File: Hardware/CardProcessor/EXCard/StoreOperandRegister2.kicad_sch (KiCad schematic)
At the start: 2 parts, among them U14 74ABT16374

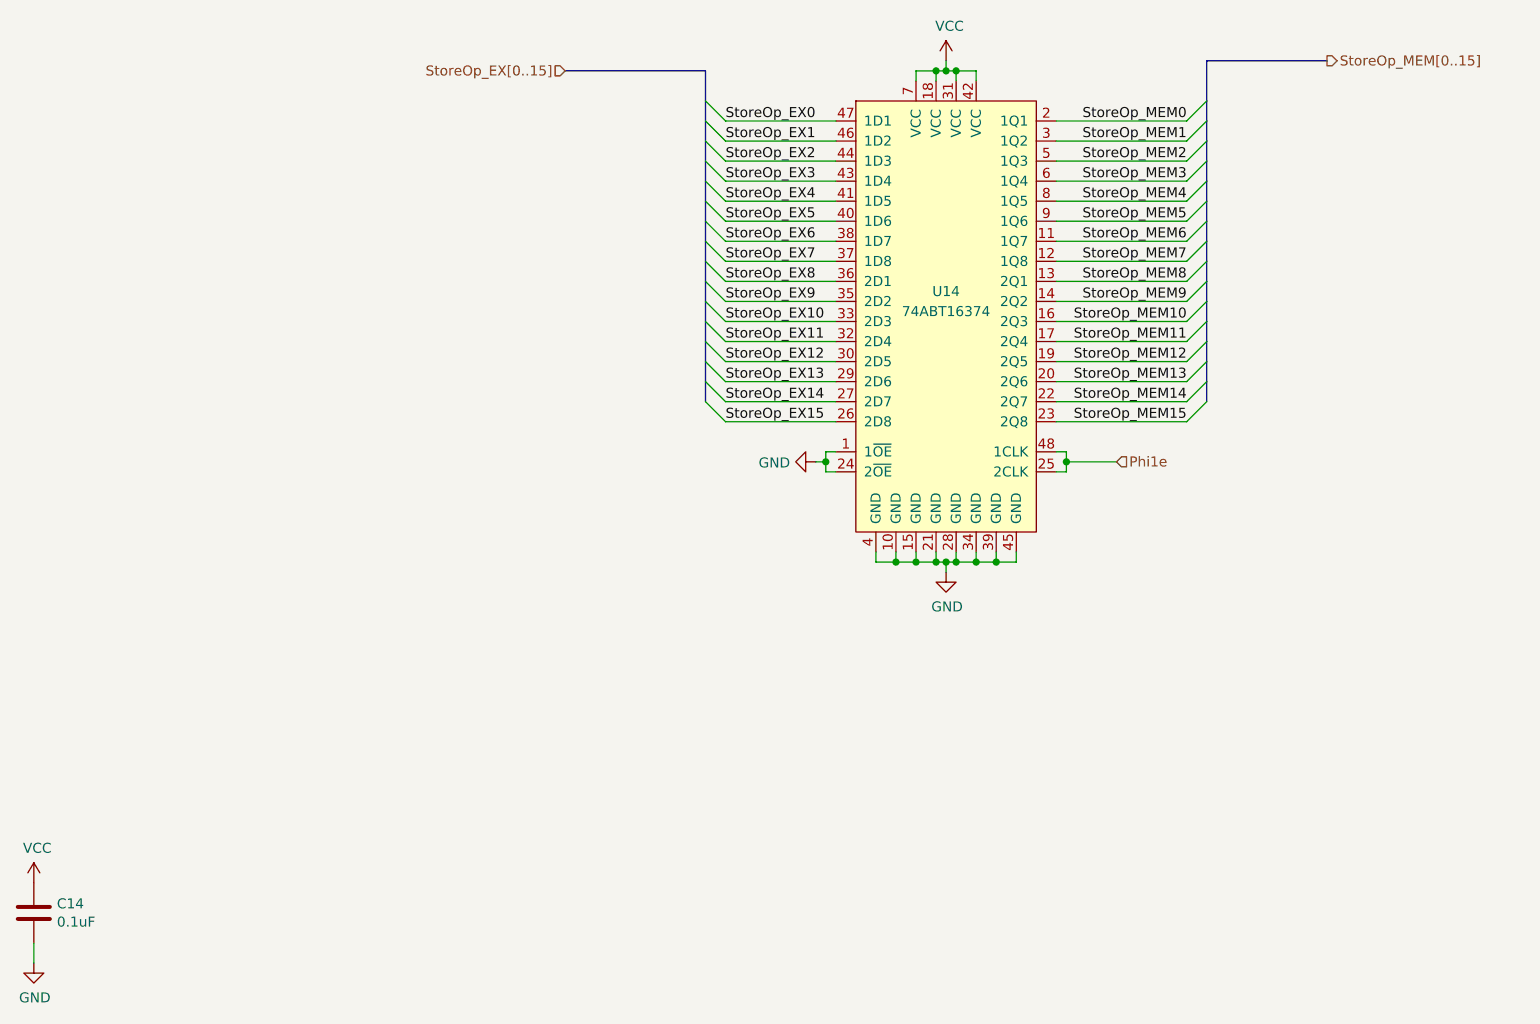
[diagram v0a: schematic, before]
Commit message: Add Turtle16Computer, a KiCad project which has schematics for the computer as a whole
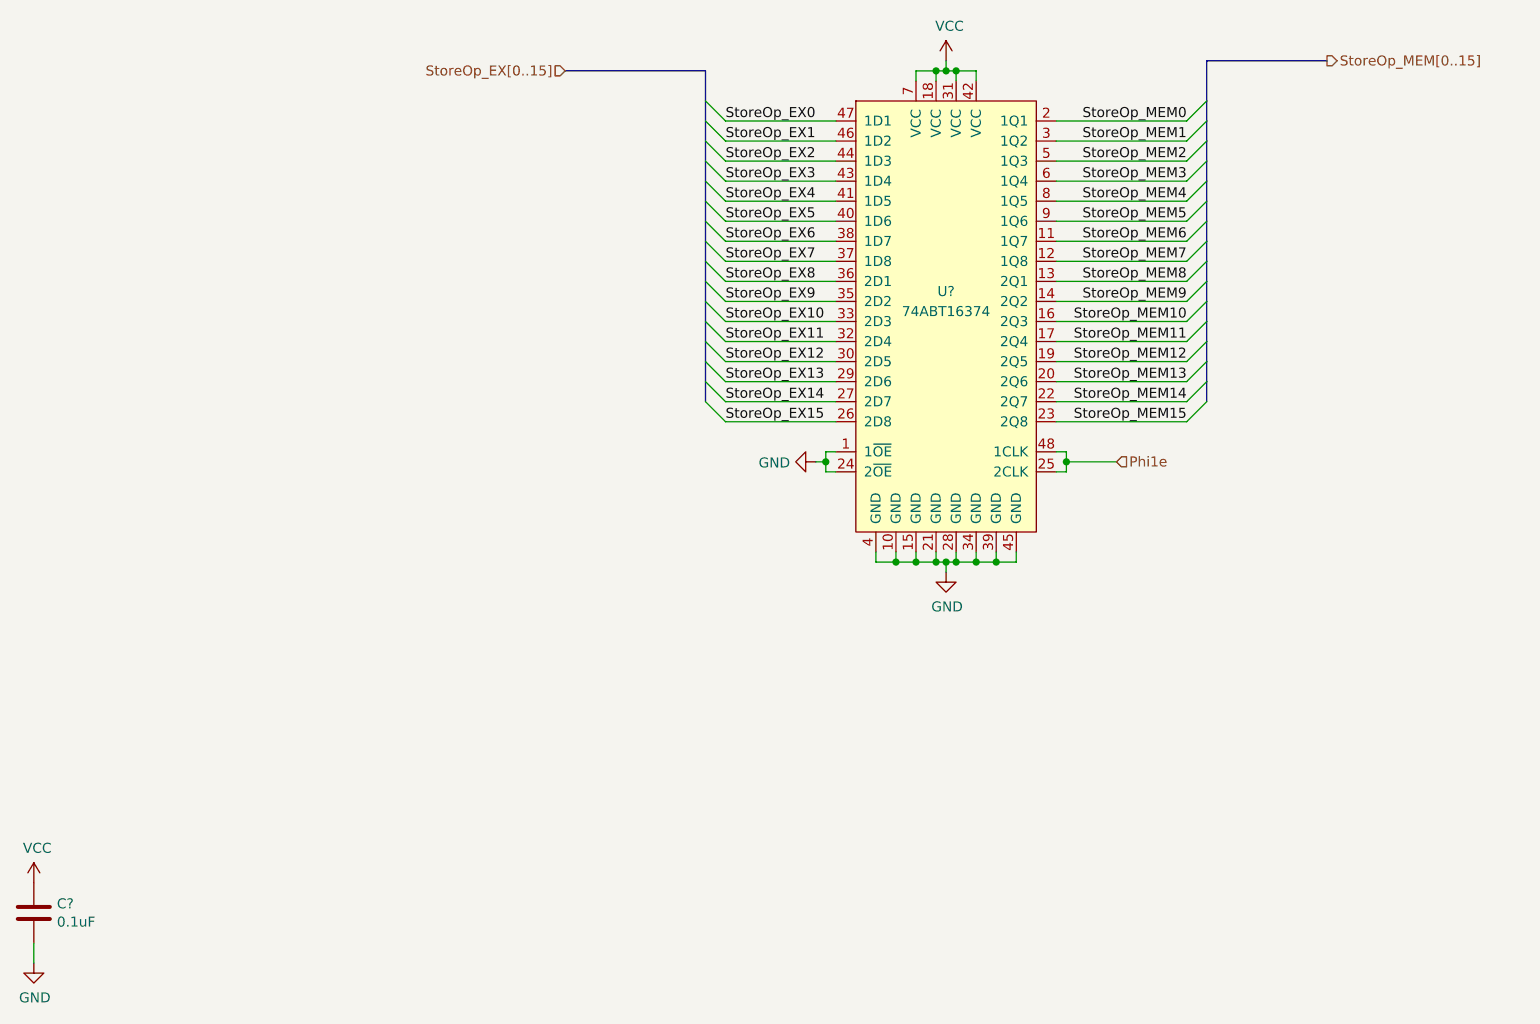
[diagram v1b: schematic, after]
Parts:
- renumbered C14 to C?, U14 to U?
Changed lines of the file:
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@@
 		(on_board yes)
 		(dnp no)
-		(property "Reference" "C14"
+		(property "Reference" "C?"
 			(at 32.131 177.9016 0)
 			(effects
@@
 		(instances
 			(project "EXModule"
-				(path "/83c5181e-f5ee-453c-ae5c-d7256ba8837d/43096b5e-2581-4688-8be9-9209d6e0ed88/00000000-0000-0000-0000-00005fd8d6fe"
-					(reference "C14")
+				(path "/83c5181e-f5ee-453c-ae5c-d7256ba8837d/637456a4-4ee5-48ca-bb06-9734ef3462ed/00000000-0000-0000-0000-00005fd8d6fe"
+					(reference "C?")
 					(unit 1)
 				)
@@
 		(on_board yes)
 		(dnp no)
-		(property "Reference" "#PWR064"
+		(property "Reference" "#PWR?"
 			(at 29.21 179.07 0)
 			(effects
@@
 		(instances
 			(project "EXModule"
-				(path "/83c5181e-f5ee-453c-ae5c-d7256ba8837d/43096b5e-2581-4688-8be9-9209d6e0ed88/00000000-0000-0000-0000-00005fd8d6fe"
-					(reference "#PWR064")
+				(path "/83c5181e-f5ee-453c-ae5c-d7256ba8837d/637456a4-4ee5-48ca-bb06-9734ef3462ed/00000000-0000-0000-0000-00005fd8d6fe"
+					(reference "#PWR?")
 					(unit 1)
 				)
@@
 		(on_board yes)
 		(dnp no)
-		(property "Reference" "#PWR065"
+		(property "Reference" "#PWR?"
 			(at 29.21 191.77 0)
 			(effects
@@
 		(instances
 			(project "EXModule"
-				(path "/83c5181e-f5ee-453c-ae5c-d7256ba8837d/43096b5e-2581-4688-8be9-9209d6e0ed88/00000000-0000-0000-0000-00005fd8d6fe"
-					(reference "#PWR065")
+				(path "/83c5181e-f5ee-453c-ae5c-d7256ba8837d/637456a4-4ee5-48ca-bb06-9734ef3462ed/00000000-0000-0000-0000-00005fd8d6fe"
+					(reference "#PWR?")
 					(unit 1)
 				)
@@
 		(on_board yes)
 		(dnp no)
-		(property "Reference" "#PWR066"
+		(property "Reference" "#PWR?"
 			(at 121.92 121.92 0)
 			(effects
@@
 		(instances
 			(project "EXModule"
-				(path "/83c5181e-f5ee-453c-ae5c-d7256ba8837d/43096b5e-2581-4688-8be9-9209d6e0ed88/00000000-0000-0000-0000-00005fd8d6fe"
-					(reference "#PWR066")
+				(path "/83c5181e-f5ee-453c-ae5c-d7256ba8837d/637456a4-4ee5-48ca-bb06-9734ef3462ed/00000000-0000-0000-0000-00005fd8d6fe"
+					(reference "#PWR?")
 					(unit 1)
 				)
@@
 		(on_board yes)
 		(dnp no)
-		(property "Reference" "#PWR067"
+		(property "Reference" "#PWR?"
 			(at 144.78 74.93 0)
 			(effects
@@
 		(instances
 			(project "EXModule"
-				(path "/83c5181e-f5ee-453c-ae5c-d7256ba8837d/43096b5e-2581-4688-8be9-9209d6e0ed88/00000000-0000-0000-0000-00005fd8d6fe"
-					(reference "#PWR067")
+				(path "/83c5181e-f5ee-453c-ae5c-d7256ba8837d/637456a4-4ee5-48ca-bb06-9734ef3462ed/00000000-0000-0000-0000-00005fd8d6fe"
+					(reference "#PWR?")
 					(unit 1)
 				)
@@
 		(on_board yes)
 		(dnp no)
-		(property "Reference" "#PWR068"
+		(property "Reference" "#PWR?"
 			(at 144.78 142.24 0)
 			(effects
@@
 		(instances
 			(project "EXModule"
-				(path "/83c5181e-f5ee-453c-ae5c-d7256ba8837d/43096b5e-2581-4688-8be9-9209d6e0ed88/00000000-0000-0000-0000-00005fd8d6fe"
-					(reference "#PWR068")
+				(path "/83c5181e-f5ee-453c-ae5c-d7256ba8837d/637456a4-4ee5-48ca-bb06-9734ef3462ed/00000000-0000-0000-0000-00005fd8d6fe"
+					(reference "#PWR?")
 					(unit 1)
 				)
@@
 		(on_board yes)
 		(dnp no)
-		(property "Reference" "U14"
+		(property "Reference" "U?"
 			(at 144.78 100.33 0)
 			(effects
@@
 		(instances
 			(project "EXModule"
-				(path "/83c5181e-f5ee-453c-ae5c-d7256ba8837d/43096b5e-2581-4688-8be9-9209d6e0ed88/00000000-0000-0000-0000-00005fd8d6fe"
-					(reference "U14")
-					(unit 1)
-				)
+				(path "/83c5181e-f5ee-453c-ae5c-d7256ba8837d/637456a4-4ee5-48ca-bb06-9734ef3462ed/00000000-0000-0000-0000-00005fd8d6fe"
+					(reference "U?")
+					(unit 1)
+				)

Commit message: Make sure all card KiCad projects pass ERC and DRC
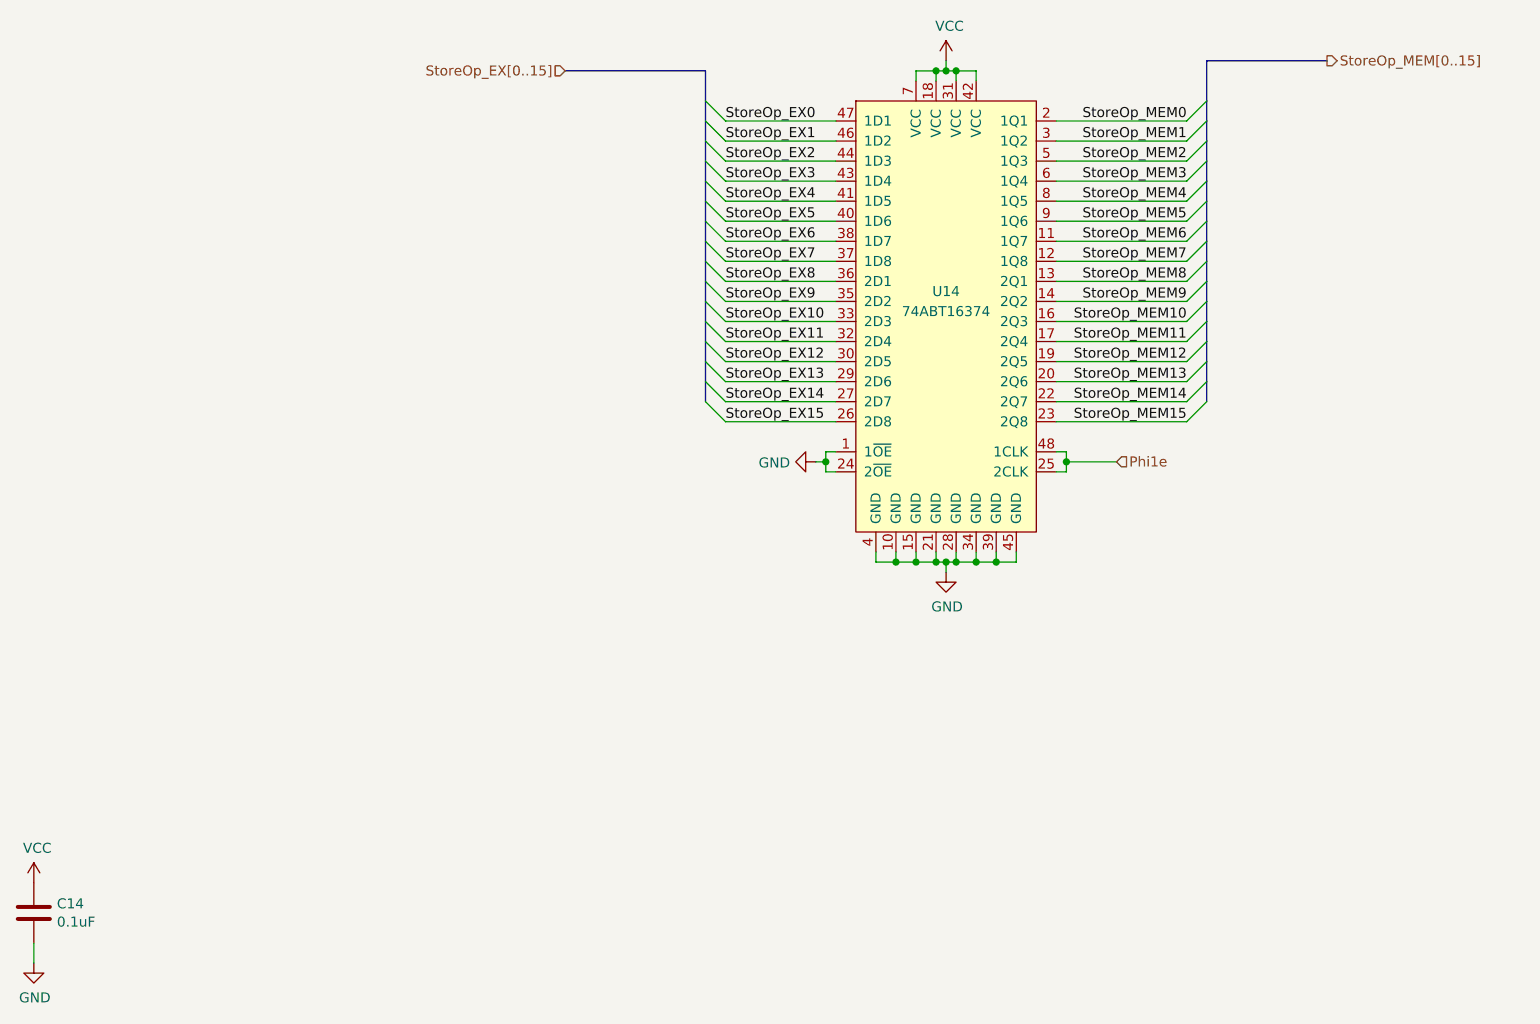
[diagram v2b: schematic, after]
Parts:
- gave numbers to parts that had none: 2
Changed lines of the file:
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@@
 		(on_board yes)
 		(dnp no)
-		(property "Reference" "C?"
+		(property "Reference" "C14"
 			(at 32.131 177.9016 0)
 			(effects
@@
 		)
 		(instances
-			(project "EXModule"
-				(path "/83c5181e-f5ee-453c-ae5c-d7256ba8837d/637456a4-4ee5-48ca-bb06-9734ef3462ed/00000000-0000-0000-0000-00005fd8d6fe"
-					(reference "C?")
+			(project "EXCard"
+				(path "/83c5181e-f5ee-453c-ae5c-d7256ba8837d/43096b5e-2581-4688-8be9-9209d6e0ed88/00000000-0000-0000-0000-00005fd8d6fe"
+					(reference "C14")
 					(unit 1)
 				)
@@
 		(on_board yes)
 		(dnp no)
-		(property "Reference" "#PWR?"
+		(property "Reference" "#PWR0272"
 			(at 29.21 179.07 0)
 			(effects
@@
 		)
 		(instances
-			(project "EXModule"
-				(path "/83c5181e-f5ee-453c-ae5c-d7256ba8837d/637456a4-4ee5-48ca-bb06-9734ef3462ed/00000000-0000-0000-0000-00005fd8d6fe"
-					(reference "#PWR?")
+			(project "EXCard"
+				(path "/83c5181e-f5ee-453c-ae5c-d7256ba8837d/43096b5e-2581-4688-8be9-9209d6e0ed88/00000000-0000-0000-0000-00005fd8d6fe"
+					(reference "#PWR0272")
 					(unit 1)
 				)
@@
 		(on_board yes)
 		(dnp no)
-		(property "Reference" "#PWR?"
+		(property "Reference" "#PWR0273"
 			(at 29.21 191.77 0)
 			(effects
@@
 		)
 		(instances
-			(project "EXModule"
-				(path "/83c5181e-f5ee-453c-ae5c-d7256ba8837d/637456a4-4ee5-48ca-bb06-9734ef3462ed/00000000-0000-0000-0000-00005fd8d6fe"
-					(reference "#PWR?")
+			(project "EXCard"
+				(path "/83c5181e-f5ee-453c-ae5c-d7256ba8837d/43096b5e-2581-4688-8be9-9209d6e0ed88/00000000-0000-0000-0000-00005fd8d6fe"
+					(reference "#PWR0273")
 					(unit 1)
 				)
@@
 		(on_board yes)
 		(dnp no)
-		(property "Reference" "#PWR?"
+		(property "Reference" "#PWR0271"
 			(at 121.92 121.92 0)
 			(effects
@@
 		)
 		(instances
-			(project "EXModule"
-				(path "/83c5181e-f5ee-453c-ae5c-d7256ba8837d/637456a4-4ee5-48ca-bb06-9734ef3462ed/00000000-0000-0000-0000-00005fd8d6fe"
-					(reference "#PWR?")
+			(project "EXCard"
+				(path "/83c5181e-f5ee-453c-ae5c-d7256ba8837d/43096b5e-2581-4688-8be9-9209d6e0ed88/00000000-0000-0000-0000-00005fd8d6fe"
+					(reference "#PWR0271")
 					(unit 1)
 				)
@@
 		(on_board yes)
 		(dnp no)
-		(property "Reference" "#PWR?"
+		(property "Reference" "#PWR0270"
 			(at 144.78 74.93 0)
 			(effects
@@
 		)
 		(instances
-			(project "EXModule"
-				(path "/83c5181e-f5ee-453c-ae5c-d7256ba8837d/637456a4-4ee5-48ca-bb06-9734ef3462ed/00000000-0000-0000-0000-00005fd8d6fe"
-					(reference "#PWR?")
+			(project "EXCard"
+				(path "/83c5181e-f5ee-453c-ae5c-d7256ba8837d/43096b5e-2581-4688-8be9-9209d6e0ed88/00000000-0000-0000-0000-00005fd8d6fe"
+					(reference "#PWR0270")
 					(unit 1)
 				)
@@
 		(on_board yes)
 		(dnp no)
-		(property "Reference" "#PWR?"
+		(property "Reference" "#PWR0269"
 			(at 144.78 142.24 0)
 			(effects
@@
 		)
 		(instances
-			(project "EXModule"
-				(path "/83c5181e-f5ee-453c-ae5c-d7256ba8837d/637456a4-4ee5-48ca-bb06-9734ef3462ed/00000000-0000-0000-0000-00005fd8d6fe"
-					(reference "#PWR?")
+			(project "EXCard"
+				(path "/83c5181e-f5ee-453c-ae5c-d7256ba8837d/43096b5e-2581-4688-8be9-9209d6e0ed88/00000000-0000-0000-0000-00005fd8d6fe"
+					(reference "#PWR0269")
 					(unit 1)
 				)
@@
 		(on_board yes)
 		(dnp no)
-		(property "Reference" "U?"
+		(property "Reference" "U14"
 			(at 144.78 100.33 0)
 			(effects
@@
 		)
 		(instances
-			(project "EXModule"
-				(path "/83c5181e-f5ee-453c-ae5c-d7256ba8837d/637456a4-4ee5-48ca-bb06-9734ef3462ed/00000000-0000-0000-0000-00005fd8d6fe"
-					(reference "U?")
-					(unit 1)
-				)
+			(project "EXCard"
+				(path "/83c5181e-f5ee-453c-ae5c-d7256ba8837d/43096b5e-2581-4688-8be9-9209d6e0ed88/00000000-0000-0000-0000-00005fd8d6fe"
+					(reference "U14")
+					(unit 1)
+				)
